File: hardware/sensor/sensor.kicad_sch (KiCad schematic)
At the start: 35 parts, among them IC1 ATTINY202-SSN, IC2 Si4012-C1001GTR, IC3 TPS3839L30DBZR, J1 M20-9770342

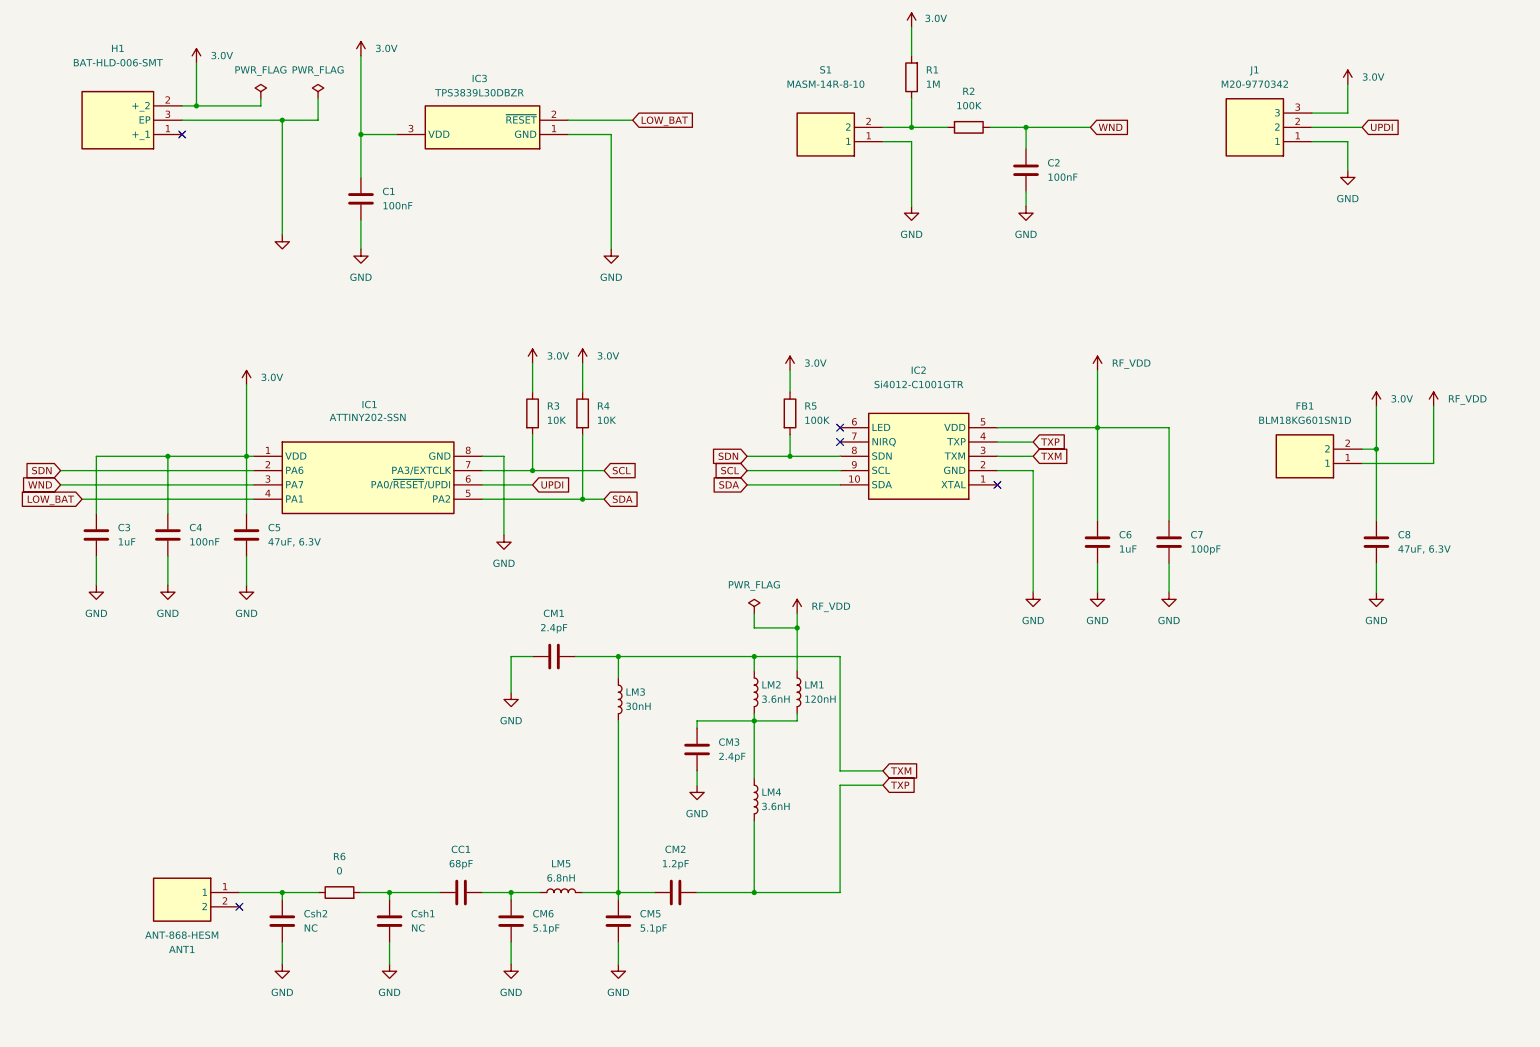
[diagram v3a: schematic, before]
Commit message: EG-29 MCU changed on schematic.
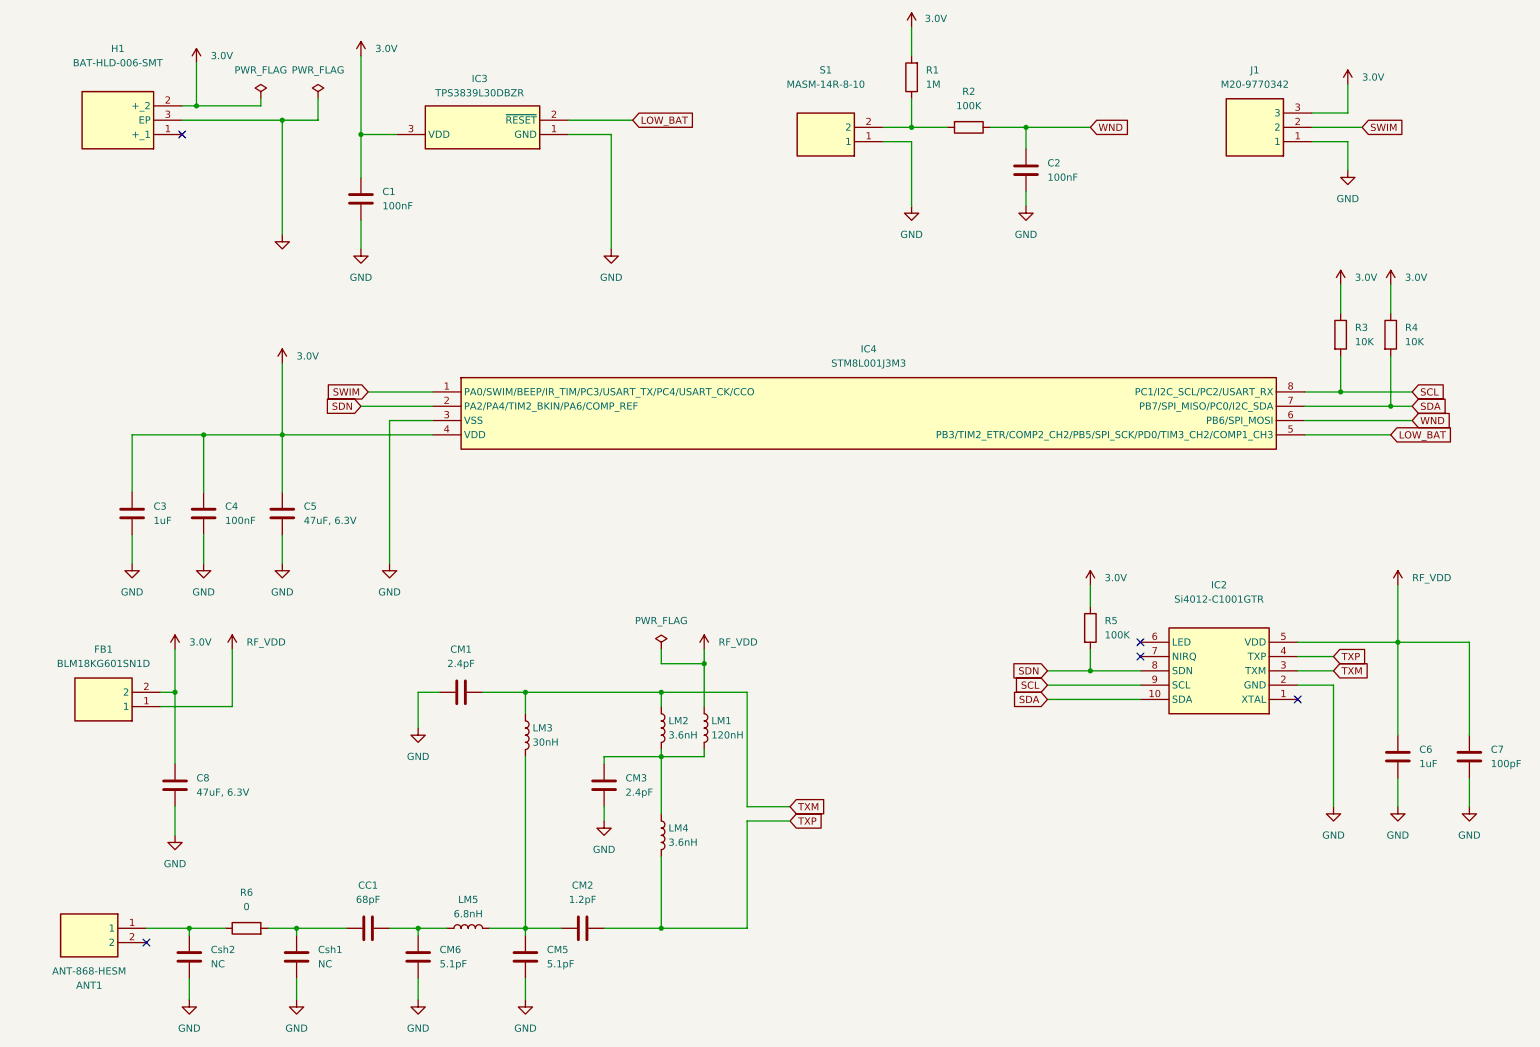
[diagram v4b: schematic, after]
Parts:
- removed IC1: ATTINY202-SSN, MyParts:SOIC127P600X175-8N, symbol ATTINY202-SSN:ATTINY202-SSN
- added IC4: STM8L001J3M3, MyParts:SOIC127P600X175-8N, symbol STM8L001J3M3:STM8L001J3M3
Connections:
- net 3.0V: now also IC4.4 (VDD)
- net GND: now also IC4.3 (VSS)
- net LOW_BAT: now also IC4.5 (PB3/TIM2_ETR/COMP2_CH2/PB5/SPI_SCK/PD0/TIM3_CH2/COMP1_CH3)
- net SCL: now also IC4.8 (PC1/I2C_SCL/PC2/USART_RX)
- net SDA: now also IC4.7 (PB7/SPI_MISO/PC0/I2C_SDA)
- net SDN: now also IC4.2 (PA2/PA4/TIM2_BKIN/PA6/COMP_REF)
- net WND: now also IC4.6 (PB6/SPI_MOSI)
- net UPDI renamed SWIM
- net SWIM: now also IC4.1 (PA0/SWIM/BEEP/IR_TIM/PC3/USART_TX/PC4/USART_CK/CCO)
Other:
- moved on the sheet: ANT1, C3, C4, C5, C6, C7, C8, CC1, CM1, CM2, CM3, CM5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

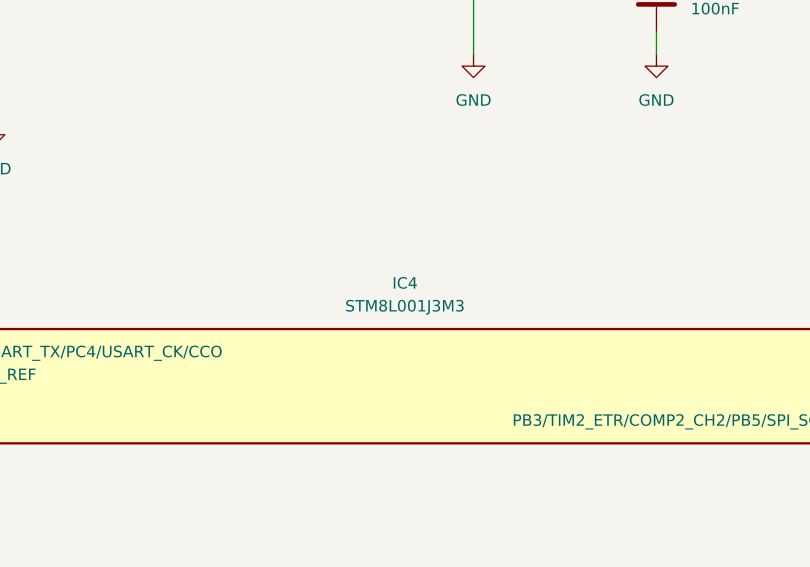
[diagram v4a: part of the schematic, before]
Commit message: EG-29 MCU changed on PCB and antenna distance fixed.
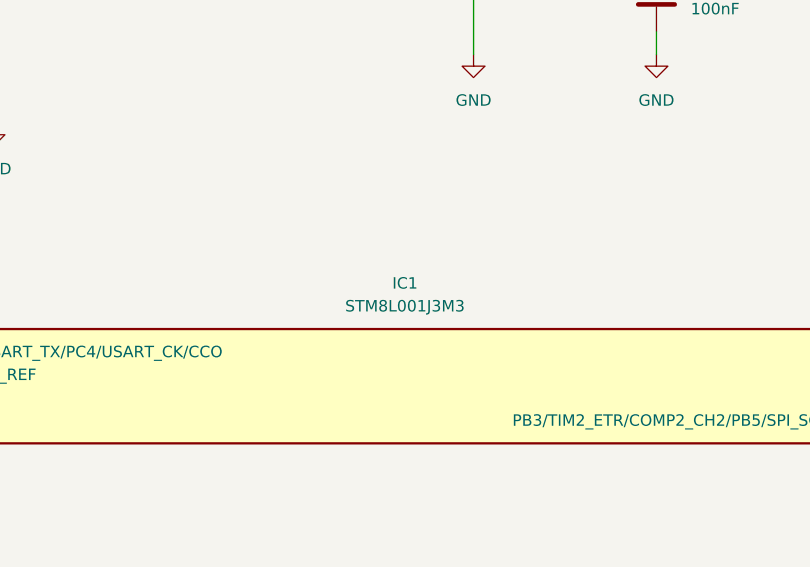
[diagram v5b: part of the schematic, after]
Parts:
- renumbered IC4 to IC1
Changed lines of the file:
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@@
 		(dnp no)
 		(fields_autoplaced yes)
-		(property "Reference" "IC4"
+		(property "Reference" "IC1"
 			(at 163.83 74.93 0)
 			(effects
@@
 			(project ""
 				(path "/0111ad26-080c-47bf-9fe6-1fe36fa86fb2"
-					(reference "IC4")
+					(reference "IC1")
 					(unit 1)
 				)

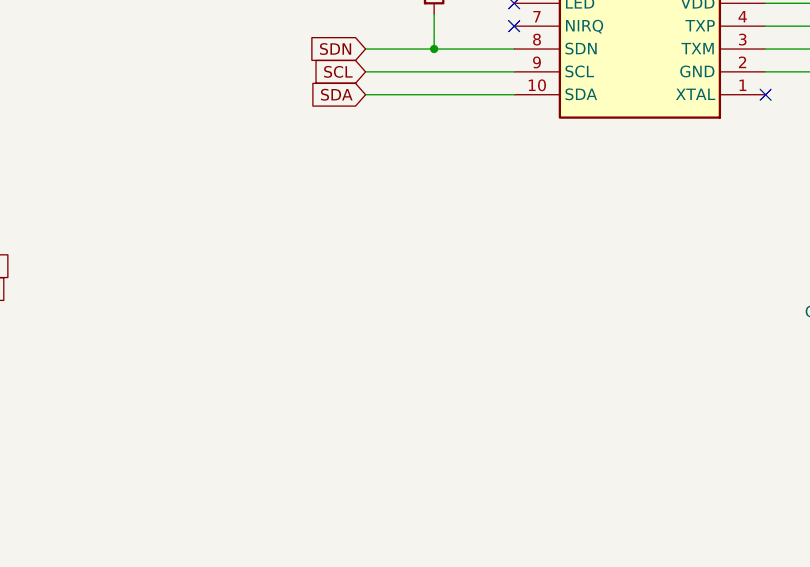
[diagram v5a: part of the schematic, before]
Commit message: EG-32 Adapted the sensor PCB for SIC5-9-2W enclosure, mainly place the holes and adjust the size of the PCB.
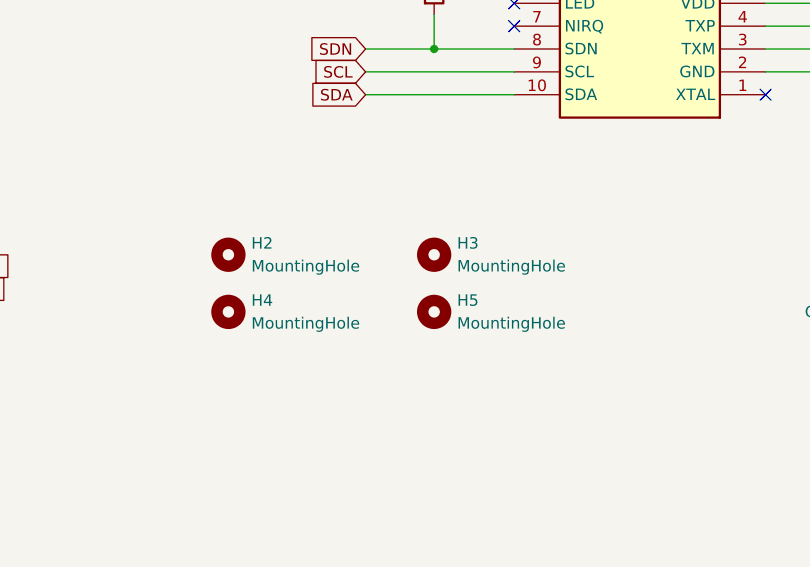
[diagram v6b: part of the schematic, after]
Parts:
- added H2, H3, H4, H5: MountingHole, MountingHole:MountingHole_2.5mm, symbol Mechanical:MountingHole

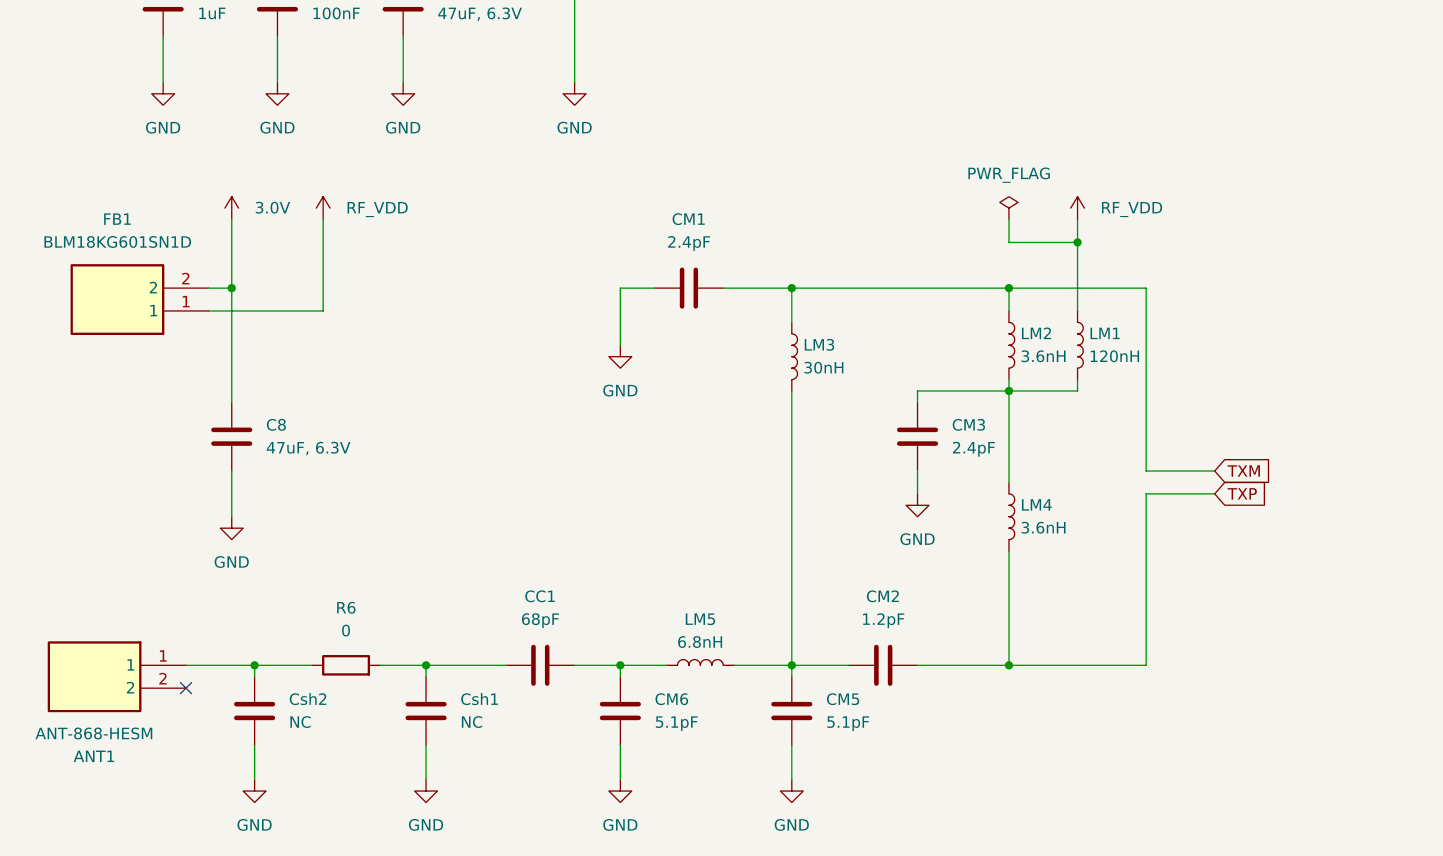
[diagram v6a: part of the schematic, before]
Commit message: EG-34 PCB antenna PI removed and added vias to connect ground planes on battery holder place.
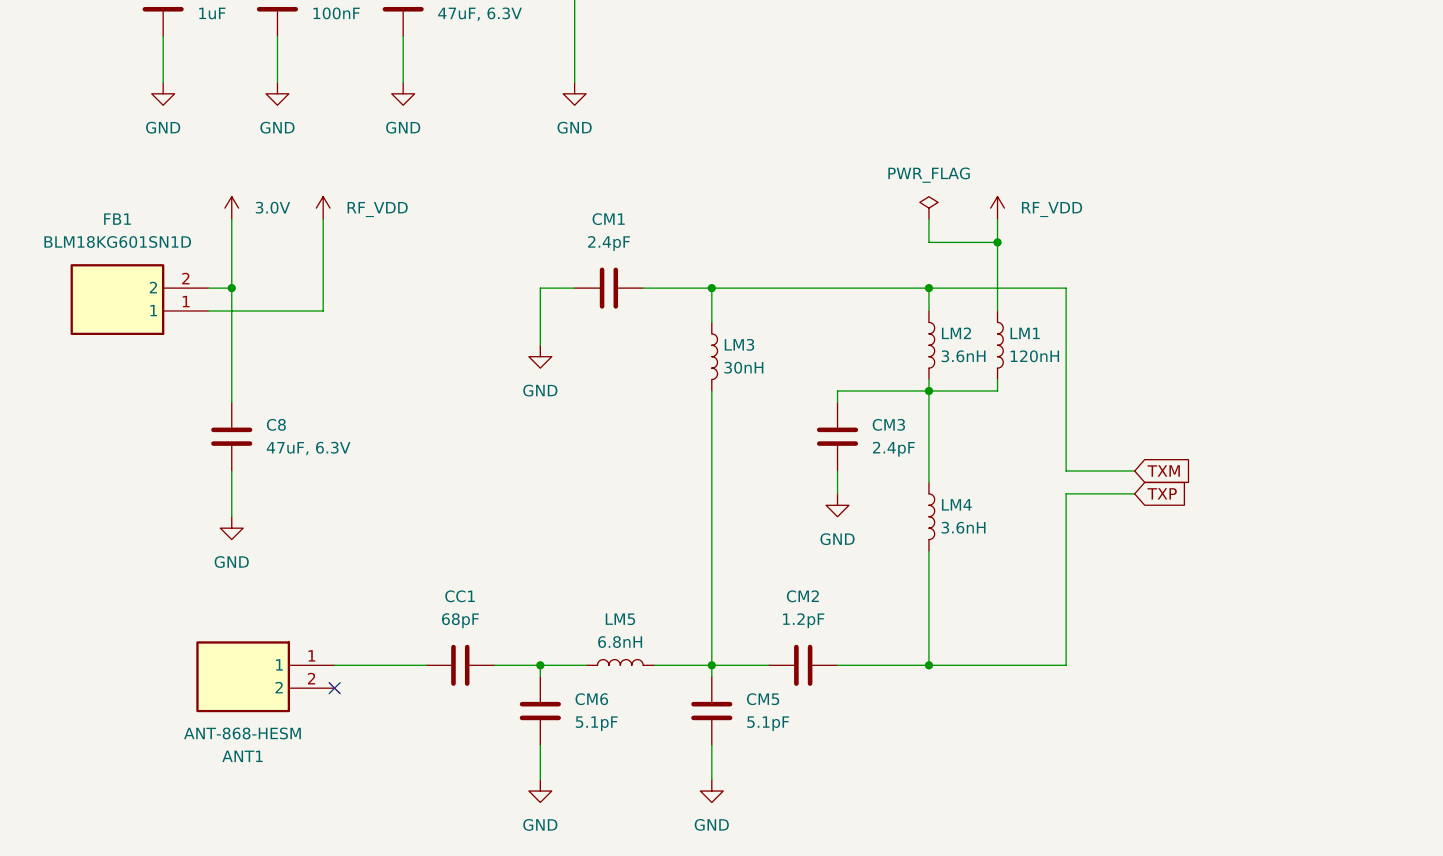
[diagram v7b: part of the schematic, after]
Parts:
- removed Csh1, Csh2: NC, Capacitor_SMD:C_0603_1608Metric, symbol Device:C
- removed R6: 0, Resistor_SMD:R_0603_1608Metric, symbol Device:R
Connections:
- net at ANT1.1: now also CC1.1
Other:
- moved on the sheet: ANT1, CC1, CM1, CM2, CM3, CM5, CM6, LM1, LM2, LM3, LM4, LM5

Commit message: EG-27 Some RF passive components replaced due to lack of stock. BOM updated.
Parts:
- CM2: Manufacturer_Name Murata -> Kyocera; Manufacturer_Part_Number GRM1555C1H1R2WA01D -> 04025A1R2DAT2A; Mouser Part Number 81-GRM1555C1H1R2WA1D -> 581-04025A1R2DAT2A; Mouser Price/Stock https://pt.mouser.com/ProductDetail/Murata-Electronics/GRM1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 -> https://pt.mouser.com/ProductDetail/KYOCERA-AVX/04025A1R2DA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
- CM5, CM6: Manufacturer_Part_Number GRM1555C1H5R1WA01D -> GCQ1555C1H5R1WB01D; Mouser Part Number 81-GRM1555C1H5R1WA1D -> 81-GCQ1555C1H5R1WB1D; Mouser Price/Stock https://eu.mouser.com/ProductDetail/Murata-Electronics/GRM1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 -> https://pt.mouser.com/ProductDetail/Murata-Electronics/GCQ1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
- LM1: Manufacturer_Name Coilcraft -> Coilcraf; Manufacturer_Part_Number 0603HP-R12XGLU -> 994-0603DC-R12XJRW; Mouser Part Number 994-0603HP-R12XGLU -> 0603DC-R12XJRW; Mouser Price/Stock https://pt.mouser.com/ProductDetail/Coilcraft/0603HP-R12XGL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 -> https://eu.mouser.com/ProductDetail/Coilcraft/0603DC-R12XJR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
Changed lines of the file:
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@@
 			)
 		)
-		(property "Mouser Part Number" "81-GRM1555C1H5R1WA1D"
+		(property "Mouser Part Number" "81-GCQ1555C1H5R1WB1D"
 			(at 93.98 182.88 0)
 			(effects
@@
 			)
 		)
-		(property "Mouser Price/Stock" "https://eu.mouser.com/ProductDetail/Murata-Electronics/GRM1555C1H5R1WA01D?qs=ouTquLLW2S6Ac9DkjU6j%2Fw%3D%3D"
+		(property "Mouser Price/Stock" "https://pt.mouser.com/ProductDetail/Murata-Electronics/GCQ1555C1H5R1WB01D?qs=0lQeLiL1qyb1w9RbymBs8A%3D%3D"
 			(at 93.98 182.88 0)
 			(effects
@@
 			)
 		)
-		(property "Manufacturer_Part_Number" "GRM1555C1H5R1WA01D"
+		(property "Manufacturer_Part_Number" "GCQ1555C1H5R1WB01D"
 			(at 93.98 182.88 0)
 			(effects
@@
 			)
 		)
-		(property "Mouser Part Number" "994-0603HP-R12XGLU"
+		(property "Mouser Part Number" "0603DC-R12XJRW"
 			(at 125.73 142.24 0)
 			(effects
@@
 			)
 		)
-		(property "Mouser Price/Stock" "https://pt.mouser.com/ProductDetail/Coilcraft/0603HP-R12XGLU?qs=zCSbvcPd3pbJT9Wmlao8cg%3D%3D"
+		(property "Mouser Price/Stock" "https://eu.mouser.com/ProductDetail/Coilcraft/0603DC-R12XJRW?qs=KUoIvG%2F9IlbgwNB48TnBTw%3D%3D"
 			(at 125.73 142.24 0)
 			(effects
@@
 			)
 		)
-		(property "Manufacturer_Name" "Coilcraft"
+		(property "Manufacturer_Name" "Coilcraf"
 			(at 125.73 142.24 0)
 			(effects
@@
 			)
 		)
-		(property "Manufacturer_Part_Number" "0603HP-R12XGLU"
+		(property "Manufacturer_Part_Number" "994-0603DC-R12XJRW"
 			(at 125.73 142.24 0)
 			(effects
@@
 			)
 		)
-		(property "Mouser Part Number" "81-GRM1555C1H1R2WA1D"
+		(property "Mouser Part Number" "581-04025A1R2DAT2A"
 			(at 104.14 177.8 90)
 			(effects
@@
 			)
 		)
-		(property "Mouser Price/Stock" "https://pt.mouser.com/ProductDetail/Murata-Electronics/GRM1555C1H1R2WA01D?qs=ouTquLLW2S4ZARlph37hBQ%3D%3D"
+		(property "Mouser Price/Stock" "https://pt.mouser.com/ProductDetail/KYOCERA-AVX/04025A1R2DAT2A?qs=vQavLFFWqfz%252Ba9yV8qz9Hg%3D%3D"
 			(at 104.14 177.8 90)
 			(effects
@@
 			)
 		)
-		(property "Manufacturer_Name" "Murata"
+		(property "Manufacturer_Name" "Kyocera"
 			(at 104.14 177.8 90)
 			(effects
@@
 			)
 		)
-		(property "Manufacturer_Part_Number" "GRM1555C1H1R2WA01D"
+		(property "Manufacturer_Part_Number" "04025A1R2DAT2A"
 			(at 104.14 177.8 90)
 			(effects
@@
 			)
 		)
-		(property "Mouser Part Number" "81-GRM1555C1H5R1WA1D"
+		(property "Mouser Part Number" "81-GCQ1555C1H5R1WB1D"
 			(at 74.93 182.88 0)
 			(effects
@@
 			)
 		)
-		(property "Mouser Price/Stock" "https://eu.mouser.com/ProductDetail/Murata-Electronics/GRM1555C1H5R1WA01D?qs=ouTquLLW2S6Ac9DkjU6j%2Fw%3D%3D"
+		(property "Mouser Price/Stock" "https://pt.mouser.com/ProductDetail/Murata-Electronics/GCQ1555C1H5R1WB01D?qs=0lQeLiL1qyb1w9RbymBs8A%3D%3D"
 			(at 74.93 182.88 0)
 			(effects
@@
 			)
 		)
-		(property "Manufacturer_Part_Number" "GRM1555C1H5R1WA01D"
+		(property "Manufacturer_Part_Number" "GCQ1555C1H5R1WB01D"
 			(at 74.93 182.88 0)
 			(effects
